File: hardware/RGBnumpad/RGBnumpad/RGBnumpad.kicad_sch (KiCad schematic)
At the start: 38 parts, among them U1 IS31FL3733-TQ

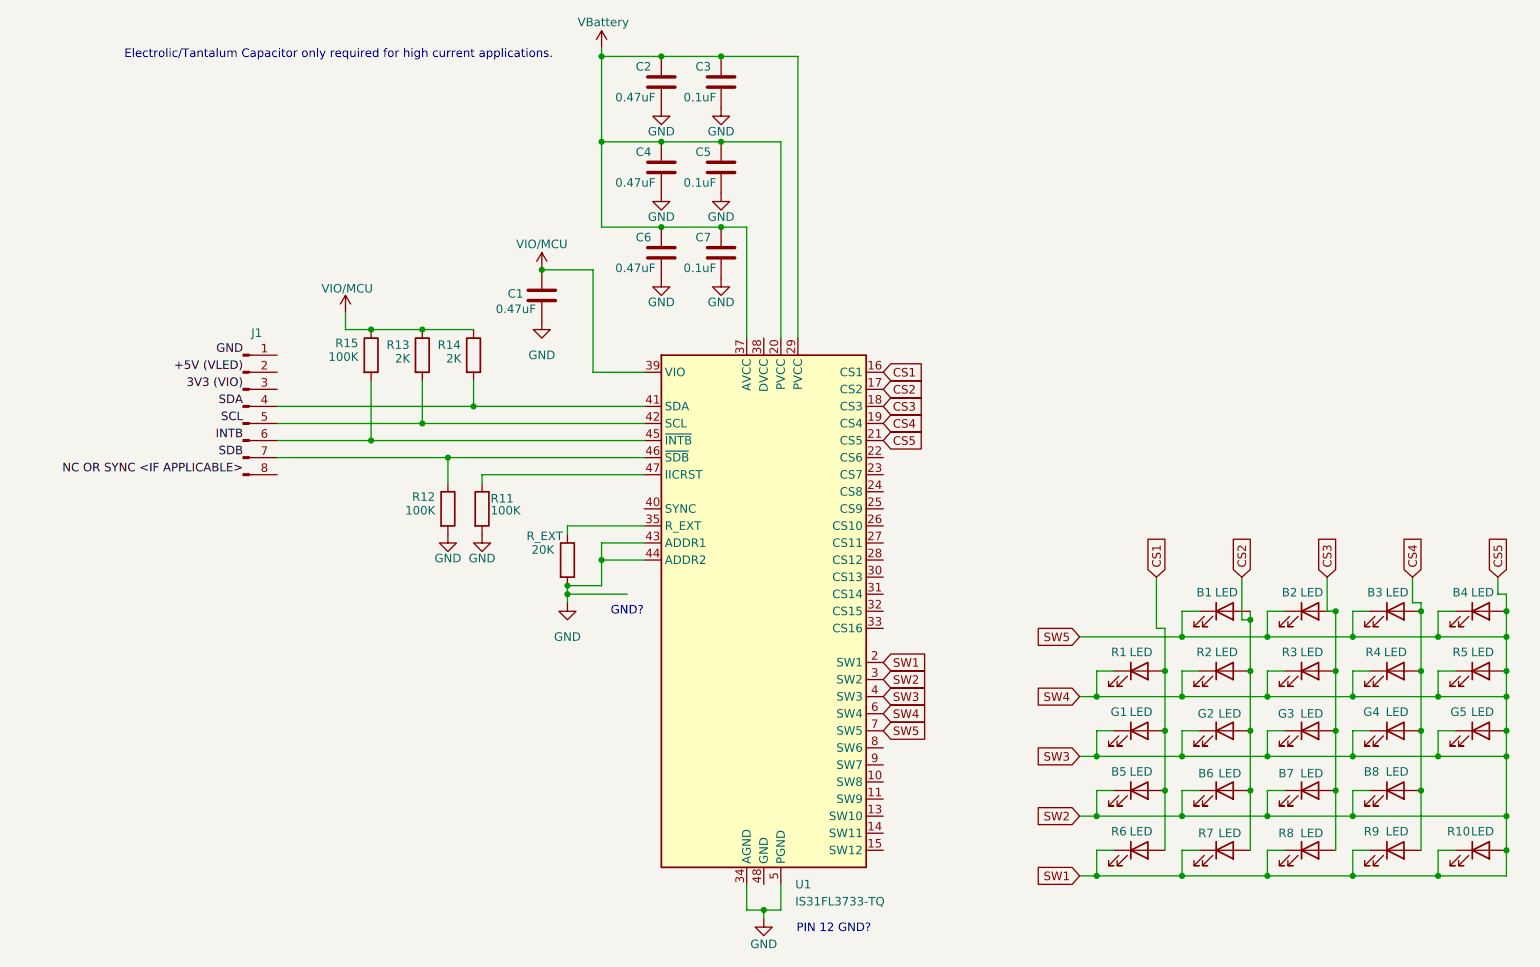
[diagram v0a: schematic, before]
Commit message: RGBnumpad Footprint
SMD 0805 hand solder footprints assigned to all of the parts on schematic
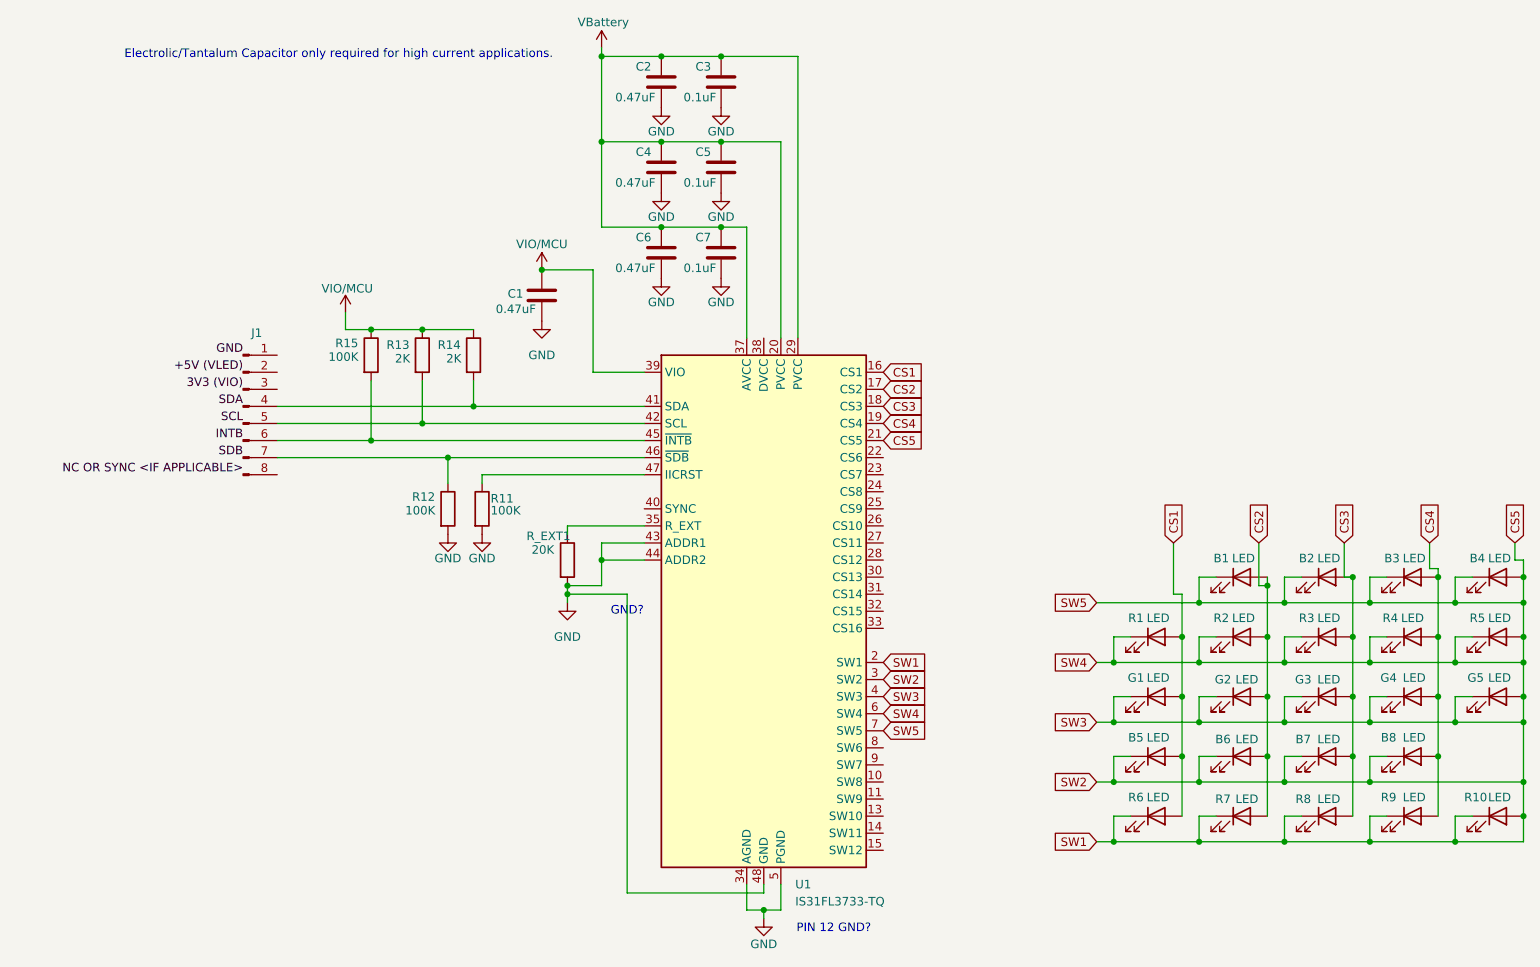
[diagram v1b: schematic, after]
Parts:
- B1, B2, B3, B4, B5, B6, B7, B8, G1, G2, G3, G4, G5, R1, R10, R2, R3, R4, R5, R6, R7, R8, R9: footprint (none) -> LED_SMD:LED_0805_2012Metric_Pad1.15x1.40mm_HandSolder
- C1, C2, C3, C4, C5, C6, C7: footprint (none) -> Capacitor_SMD:C_0805_2012Metric_Pad1.18x1.45mm_HandSolder
- R11, R12, R13, R14, R15: footprint (none) -> Resistor_SMD:R_0805_2012Metric_Pad1.20x1.40mm_HandSolder
- R_EXT1: renamed from R_EXT; footprint (none) -> Resistor_SMD:R_0805_2012Metric_Pad1.20x1.40mm_HandSolder
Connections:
- net GND: now also U1.48 (GND), U1.49 (GND)
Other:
- moved on the sheet: B1, B2, B3, B4, B5, B6, B7, B8, G1, G2, G3, G4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
